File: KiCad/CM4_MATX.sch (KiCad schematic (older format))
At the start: 0 parts

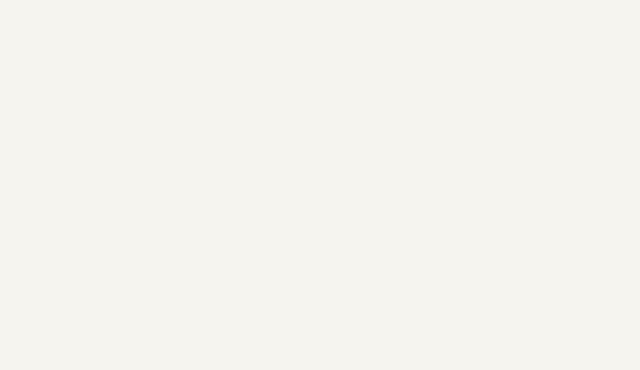
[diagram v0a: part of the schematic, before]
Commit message: added mounting holes to CM4_MATX.sch
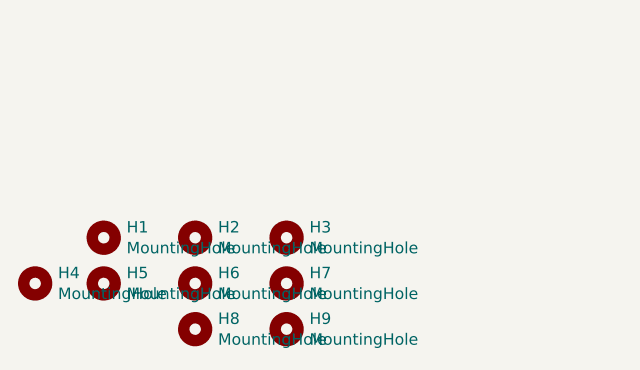
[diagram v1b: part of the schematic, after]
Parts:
- added H1, H2, H3, H4, H5, H6, H7, H8, H9: MountingHole, MountingHole:MountingHole_3.2mm_M3, symbol Mechanical:MountingHole
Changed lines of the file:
@@
 F1 "CM4_USB2_HUB.sch" 50
 $EndSheet
+$Comp
+L Mechanical:MountingHole H1
+U 1 1 5FB6444A
+P 1150 7200
+F 0 "H1" H 1250 7246 50  0000 L CNN
+F 1 "MountingHole" H 1250 7155 50  0000 L CNN
+F 2 "MountingHole:MountingHole_3.2mm_M3" H 1150 7200 50  0001 C CNN
+F 3 "~" H 1150 7200 50  0001 C CNN
+	1    1150 7200
+	1    0    0    -1
+$EndComp
+$Comp
+L Mechanical:MountingHole H2
+U 1 1 5FB649F9
+P 1550 7200
+F 0 "H2" H 1650 7246 50  0000 L CNN
+F 1 "MountingHole" H 1650 7155 50  0000 L CNN
+F 2 "MountingHole:MountingHole_3.2mm_M3" H 1550 7200 50  0001 C CNN
+F 3 "~" H 1550 7200 50  0001 C CNN
+	1    1550 7200
+	1    0    0    -1
+$EndComp
+$Comp
+L Mechanical:MountingHole H3
+U 1 1 5FB64C61
+P 1950 7200
+F 0 "H3" H 2050 7246 50  0000 L CNN
+F 1 "MountingHole" H 2050 7155 50  0000 L CNN
+F 2 "MountingHole:MountingHole_3.2mm_M3" H 1950 7200 50  0001 C CNN
+F 3 "~" H 1950 7200 50  0001 C CNN
+	1    1950 7200
+	1    0    0    -1
+$EndComp
+$Comp
+L Mechanical:MountingHole H4
+U 1 1 5FB658C2
+P 850 7400
+F 0 "H4" H 950 7446 50  0000 L CNN
+F 1 "MountingHole" H 950 7355 50  0000 L CNN
+F 2 "MountingHole:MountingHole_3.2mm_M3" H 850 7400 50  0001 C CNN
+F 3 "~" H 850 7400 50  0001 C CNN
+	1    850  7400
+	1    0    0    -1
+$EndComp
+$Comp
+L Mechanical:MountingHole H5
+U 1 1 5FB65A47
+P 1150 7400
+F 0 "H5" H 1250 7446 50  0000 L CNN
+F 1 "MountingHole" H 1250 7355 50  0000 L CNN
+F 2 "MountingHole:MountingHole_3.2mm_M3" H 1150 7400 50  0001 C CNN
+F 3 "~" H 1150 7400 50  0001 C CNN
+	1    1150 7400
+	1    0    0    -1
+$EndComp
+$Comp
+L Mechanical:MountingHole H6
+U 1 1 5FB65B17
+P 1550 7400
+F 0 "H6" H 1650 7446 50  0000 L CNN
+F 1 "MountingHole" H 1650 7355 50  0000 L CNN
+F 2 "MountingHole:MountingHole_3.2mm_M3" H 1550 7400 50  0001 C CNN
+F 3 "~" H 1550 7400 50  0001 C CNN
+	1    1550 7400
+	1    0    0    -1
+$EndComp
+$Comp
+L Mechanical:MountingHole H7
+U 1 1 5FB65D40
+P 1950 7400
+F 0 "H7" H 2050 7446 50  0000 L CNN
+F 1 "MountingHole" H 2050 7355 50  0000 L CNN
+F 2 "MountingHole:MountingHole_3.2mm_M3" H 1950 7400 50  0001 C CNN
+F 3 "~" H 1950 7400 50  0001 C CNN
+	1    1950 7400
+	1    0    0    -1
+$EndComp
+$Comp
+L Mechanical:MountingHole H9
+U 1 1 5FB65FD3
+P 1950 7600
+F 0 "H9" H 2050 7646 50  0000 L CNN
+F 1 "MountingHole" H 2050 7555 50  0000 L CNN
+F 2 "MountingHole:MountingHole_3.2mm_M3" H 1950 7600 50  0001 C CNN
+F 3 "~" H 1950 7600 50  0001 C CNN
+	1    1950 7600
+	1    0    0    -1
+$EndComp
+$Comp
+L Mechanical:MountingHole H8
+U 1 1 5FB66182
+P 1550 7600
+F 0 "H8" H 1650 7646 50  0000 L CNN
+F 1 "MountingHole" H 1650 7555 50  0000 L CNN
+F 2 "MountingHole:MountingHole_3.2mm_M3" H 1550 7600 50  0001 C CNN
+F 3 "~" H 1550 7600 50  0001 C CNN
+	1    1550 7600
+	1    0    0    -1
+$EndComp
 $EndSCHEMATC

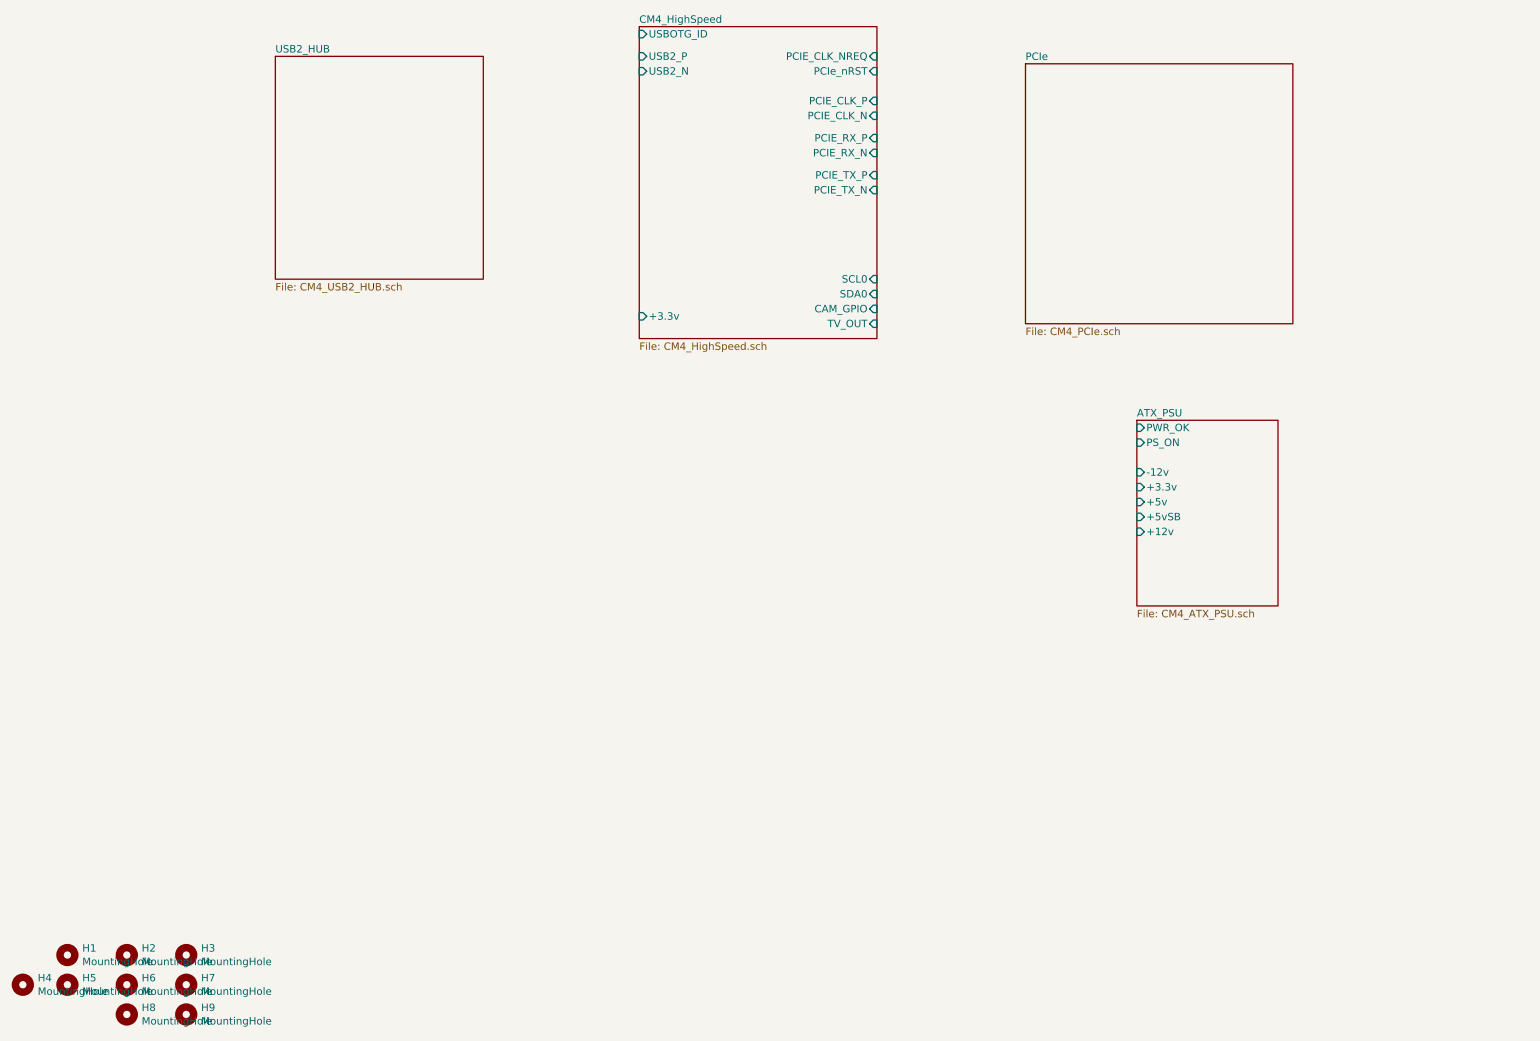
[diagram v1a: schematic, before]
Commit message: Lotsa changes
Added new footprints:
PCIe x1, TO-252 tab, SOT95, SOP50, SON50, Hirose FH-12-22S, 2.54mm 2x02 and 2x05 headers
Added new models:
Hirose FH-12-22S, FSUSB42MUX, MIC2019YM6-TR, TPS6206
Re-did ATX connector symbol wiring
Begun wiring PI7C PCI-e switch
Wired USB2517 hub
Begun adding MIC2019YM6 current limiters.
Added TODO lists to each page to help new contributors
Begun placing PCB footprints and descriptors
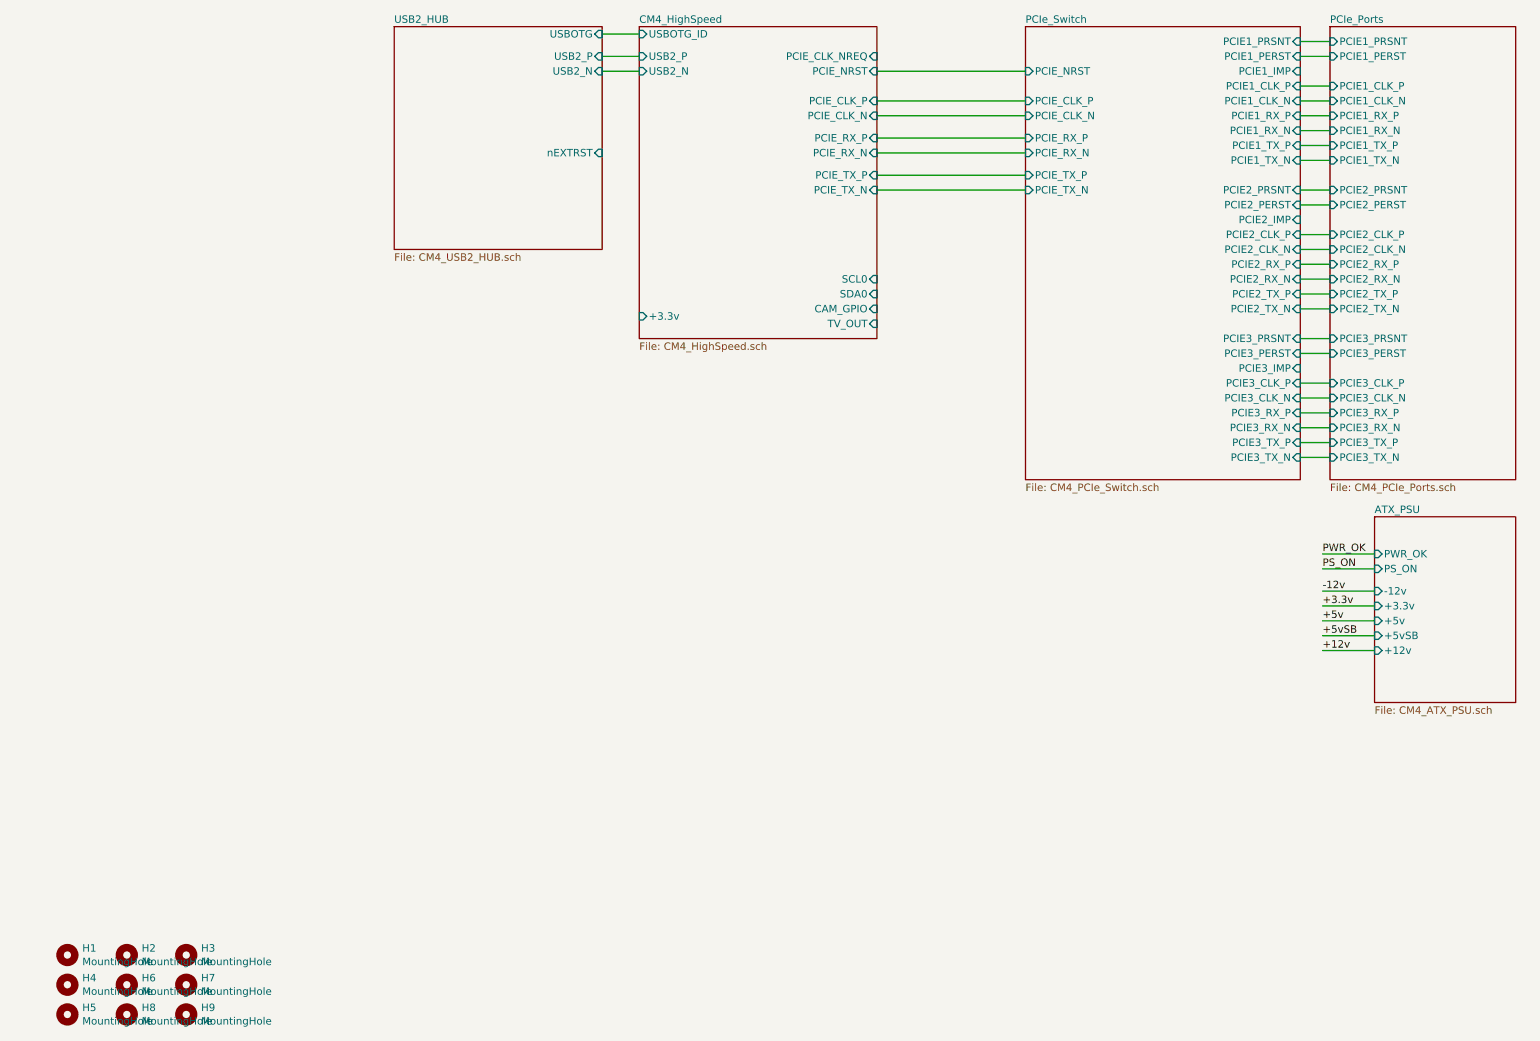
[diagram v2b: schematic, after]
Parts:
- H3: footprint MountingHole:MountingHole_3.2mm_M3 -> MountingHole:MountingHole_3.2mm_M3_Pad_Via
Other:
- moved on the sheet: H4, H5
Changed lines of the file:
@@
 $Descr A4 11693 8268
 encoding utf-8
-Sheet 1 5
+Sheet 1 6
 Title "CM4 MATX Root Sheet"
 Date "2020-11-19"
@@
 F1 "CM4_HighSpeed.sch" 50
 F2 "TV_OUT" I R 6600 2950 50
-F3 "PCIe_nRST" I R 6600 1250 50
+F3 "PCIE_NRST" I R 6600 1250 50
 F4 "USB2_P" I L 5000 1150 50
 F5 "USB2_N" I L 5000 1250 50
@@
 $EndSheet
 $Sheet
-S 8350 3600 950  1250
+S 9950 4250 950  1250
 U 5FB443D9
 F0 "ATX_PSU" 50
 F1 "CM4_ATX_PSU.sch" 50
-F2 "+3.3v" I L 8350 4050 50
-F3 "+5v" I L 8350 4150 50
-F4 "+12v" I L 8350 4350 50
-F5 "+5vSB" I L 8350 4250 50
-F6 "-12v" I L 8350 3950 50
-F7 "PS_ON" I L 8350 3750 50
-F8 "PWR_OK" I L 8350 3650 50
-$EndSheet
-$Sheet
-S 7600 1200 1800 1750
-U 5FB442B7
-F0 "PCIe" 50
-F1 "CM4_PCIe.sch" 50
-$EndSheet
-$Sheet
-S 2550 1150 1400 1500
+F2 "+3.3v" I L 9950 4850 50
+F3 "+5v" I L 9950 4950 50
+F4 "+12v" I L 9950 5150 50
+F5 "+5vSB" I L 9950 5050 50
+F6 "-12v" I L 9950 4750 50
+F7 "PS_ON" I L 9950 4600 50
+F8 "PWR_OK" I L 9950 4500 50
+$EndSheet
+$Sheet
+S 3350 950  1400 1500
 U 5FB43DAF
 F0 "USB2_HUB" 50
 F1 "CM4_USB2_HUB.sch" 50
+F2 "nEXTRST" I R 4750 1800 50
+F3 "USBOTG" I R 4750 1000 50
+F4 "USB2_P" I R 4750 1150 50
+F5 "USB2_N" I R 4750 1250 50
 $EndSheet
 $Comp
@@
 F 0 "H3" H 2050 7246 50  0000 L CNN
 F 1 "MountingHole" H 2050 7155 50  0000 L CNN
-F 2 "MountingHole:MountingHole_3.2mm_M3" H 1950 7200 50  0001 C CNN
+F 2 "MountingHole:MountingHole_3.2mm_M3_Pad_Via" H 1950 7200 50  0001 C CNN
 F 3 "~" H 1950 7200 50  0001 C CNN
 	1    1950 7200
@@
 L Mechanical:MountingHole H4
 U 1 1 5FB658C2
-P 850 7400
-F 0 "H4" H 950 7446 50  0000 L CNN
-F 1 "MountingHole" H 950 7355 50  0000 L CNN
-F 2 "MountingHole:MountingHole_3.2mm_M3" H 850 7400 50  0001 C CNN
-F 3 "~" H 850 7400 50  0001 C CNN
-	1    850  7400
-	1    0    0    -1
-$EndComp
-$Comp
-L Mechanical:MountingHole H5
-U 1 1 5FB65A47
 P 1150 7400
-F 0 "H5" H 1250 7446 50  0000 L CNN
+F 0 "H4" H 1250 7446 50  0000 L CNN
 F 1 "MountingHole" H 1250 7355 50  0000 L CNN
 F 2 "MountingHole:MountingHole_3.2mm_M3" H 1150 7400 50  0001 C CNN
 F 3 "~" H 1150 7400 50  0001 C CNN
 	1    1150 7400
+	1    0    0    -1
+$EndComp
+$Comp
+L Mechanical:MountingHole H5
+U 1 1 5FB65A47
+P 1150 7600
+F 0 "H5" H 1250 7646 50  0000 L CNN
+F 1 "MountingHole" H 1250 7555 50  0000 L CNN
+F 2 "MountingHole:MountingHole_3.2mm_M3" H 1150 7600 50  0001 C CNN
+F 3 "~" H 1150 7600 50  0001 C CNN
+	1    1150 7600
 	1    0    0    -1
 $EndComp
@@
 	1    0    0    -1
 $EndComp
+$Sheet
+S 7600 950  1850 3050
+U 5FB442B7
+F0 "PCIe_Switch" 50
+F1 "CM4_PCIe_Switch.sch" 50
+F2 "PCIE_CLK_N" I L 7600 1550 50
+F3 "PCIE_CLK_P" I L 7600 1450 50
+F4 "PCIE_RX_P" I L 7600 1700 50
+F5 "PCIE_RX_N" I L 7600 1800 50
+F6 "PCIE_TX_P" I L 7600 1950 50
+F7 "PCIE_TX_N" I L 7600 2050 50
+F8 "PCIE_NRST" I L 7600 1250 50
+F9 "PCIE1_PRSNT" I R 9450 1050 50
+F10 "PCIE2_PRSNT" I R 9450 2050 50
+F11 "PCIE3_PRSNT" I R 9450 3050 50
+F12 "PCIE1_PERST" I R 9450 1150 50
+F13 "PCIE2_PERST" I R 9450 2150 50
+F14 "PCIE3_PERST" I R 9450 3150 50
+F15 "PCIE1_IMP" I R 9450 1250 50
+F16 "PCIE2_IMP" I R 9450 2250 50
+F17 "PCIE3_IMP" I R 9450 3250 50
+F18 "PCIE3_CLK_N" I R 9450 3450 50
+F19 "PCIE3_CLK_P" I R 9450 3350 50
+F20 "PCIE2_CLK_N" I R 9450 2450 50
+F21 "PCIE2_CLK_P" I R 9450 2350 50
+F22 "PCIE1_CLK_N" I R 9450 1450 50
+F23 "PCIE1_CLK_P" I R 9450 1350 50
+F24 "PCIE1_RX_P" I R 9450 1550 50
+F25 "PCIE1_RX_N" I R 9450 1650 50
+F26 "PCIE1_TX_P" I R 9450 1750 50
+F27 "PCIE1_TX_N" I R 9450 1850 50
+F28 "PCIE2_RX_P" I R 9450 2550 50
+F29 "PCIE2_RX_N" I R 9450 2650 50
+F30 "PCIE2_TX_P" I R 9450 2750 50
+F31 "PCIE2_TX_N" I R 9450 2850 50
+F32 "PCIE3_TX_N" I R 9450 3850 50
+F33 "PCIE3_TX_P" I R 9450 3750 50
+F34 "PCIE3_RX_N" I R 9450 3650 50
+F35 "PCIE3_RX_P" I R 9450 3550 50
+$EndSheet
+Text Label 9600 4500 0    50   ~ 0
+PWR_OK
+Text Label 9600 4600 0    50   ~ 0
+PS_ON
+Text Label 9600 4850 0    50   ~ 0
++3.3v
+Text Label 9600 4950 0    50   ~ 0
++5v
+Text Label 9600 5050 0    50   ~ 0
++5vSB
+Text Label 9600 5150 0    50   ~ 0
++12v
+Wire Wire Line
+	9600 5150 9950 5150
+Wire Wire Line
+	9950 5050 9600 5050
+Wire Wire Line
+	9600 4950 9950 4950
+Wire Wire Line
+	9950 4850 9600 4850
+Wire Wire Line
+	9950 4600 9600 4600
+Wire Wire Line
+	9600 4500 9950 4500
+$Sheet
+S 9650 950  1250 3050
+U 5FCA7683
+F0 "PCIe_Ports" 50
+F1 "CM4_PCIe_Ports.sch" 50
+F2 "PCIE2_PRSNT" I L 9650 2050 50
+F3 "PCIE2_PERST" I L 9650 2150 50
+F4 "PCIE2_CLK_P" I L 9650 2350 50
+F5 "PCIE2_CLK_N" I L 9650 2450 50
+F6 "PCIE2_RX_P" I L 9650 2550 50
+F7 "PCIE2_RX_N" I L 9650 2650 50
+F8 "PCIE2_TX_N" I L 9650 2850 50
+F9 "PCIE2_TX_P" I L 9650 2750 50
+F10 "PCIE3_PRSNT" I L 9650 3050 50
+F11 "PCIE3_PERST" I L 9650 3150 50
+F12 "PCIE3_CLK_P" I L 9650 3350 50
+F13 "PCIE3_CLK_N" I L 9650 3450 50
+F14 "PCIE3_RX_N" I L 9650 3650 50
+F15 "PCIE3_RX_P" I L 9650 3550 50
+F16 "PCIE1_RX_P" I L 9650 1550 50
+F17 "PCIE1_RX_N" I L 9650 1650 50
+F18 "PCIE1_CLK_N" I L 9650 1450 50
+F19 "PCIE1_CLK_P" I L 9650 1350 50
+F20 "PCIE1_PERST" I L 9650 1150 50
+F21 "PCIE1_PRSNT" I L 9650 1050 50
+F22 "PCIE1_TX_P" I L 9650 1750 50
+F23 "PCIE1_TX_N" I L 9650 1850 50
+F24 "PCIE3_TX_P" I L 9650 3750 50
+F25 "PCIE3_TX_N" I L 9650 3850 50
+$EndSheet
+Wire Wire Line
+	9650 3850 9450 3850
+Wire Wire Line
+	9450 3750 9650 3750
+Wire Wire Line
+	9650 3650 9450 3650
+Wire Wire Line
+	9450 3550 9650 3550
+Wire Wire Line
+	9650 3450 9450 3450
+Wire Wire Line
+	9450 3350 9650 3350
+Wire Wire Line
+	9650 3150 9450 3150
+Wire Wire Line
+	9450 3050 9650 3050
+Wire Wire Line
+	9650 2850 9450 2850
+Wire Wire Line
+	9450 2750 9650 2750
+Wire Wire Line
+	9650 2650 9450 2650
+Wire Wire Line
+	9450 2550 9650 2550
+Wire Wire Line
+	9650 2450 9450 2450
+Wire Wire Line
+	9450 2350 9650 2350
+Wire Wire Line
+	9650 2150 9450 2150
+Wire Wire Line
+	9450 2050 9650 2050
+Wire Wire Line
+	9650 1850 9450 1850
+Wire Wire Line
+	9450 1750 9650 1750
+Wire Wire Line
+	9650 1650 9450 1650
+Wire Wire Line
+	9450 1550 9650 1550
+Wire Wire Line
+	9650 1450 9450 1450
+Wire Wire Line
+	9450 1350 9650 1350
+Wire Wire Line
+	9650 1150 9450 1150
+Wire Wire Line
+	9450 1050 9650 1050
+Wire Wire Line
+	7600 1250 6600 1250
+Wire Wire Line
+	6600 1450 7600 1450
+Wire Wire Line
+	7600 1550 6600 1550
+Wire Wire Line
+	6600 1700 7600 1700
+Wire Wire Line
+	7600 1800 6600 1800
+Wire Wire Line
+	6600 1950 7600 1950
+Wire Wire Line
+	7600 2050 6600 2050
+Wire Wire Line
+	4750 1250 5000 1250
+Wire Wire Line
+	5000 1150 4750 1150
+Wire Wire Line
+	4750 1000 5000 1000
+Wire Wire Line
+	9600 4750 9950 4750
+Text Label 9600 4750 0    50   ~ 0
+-12v
 $EndSCHEMATC

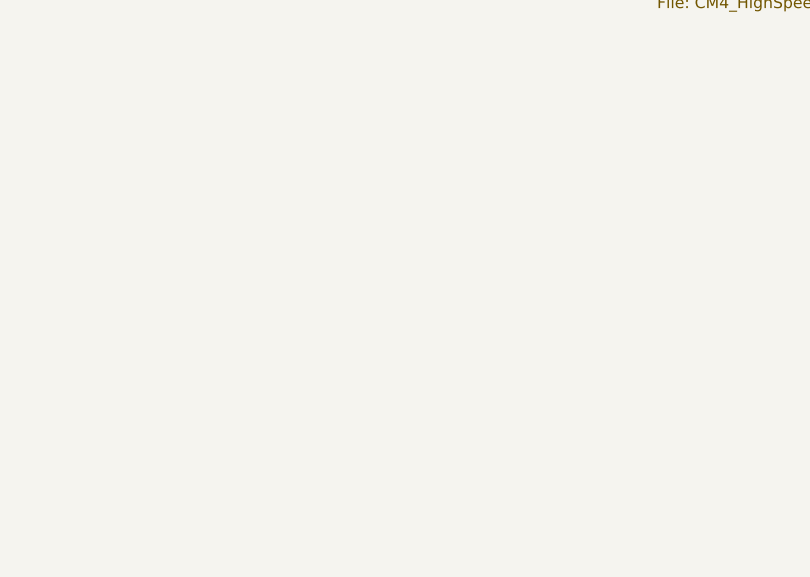
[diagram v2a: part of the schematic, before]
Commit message: added FanCRTL with MAX31740 as hierarchical sheet
with all footprints and symbols necessary
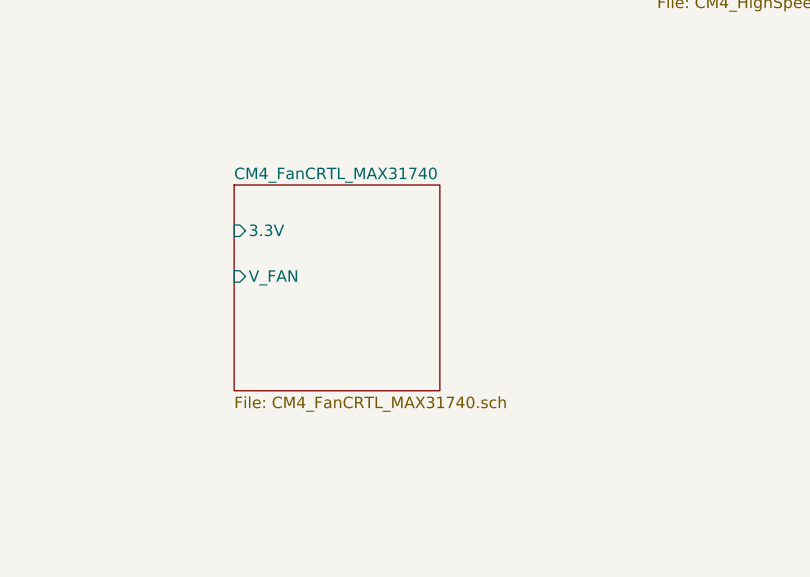
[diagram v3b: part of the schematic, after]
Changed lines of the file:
@@
 $Descr A4 11693 8268
 encoding utf-8
-Sheet 1 6
+Sheet 1 7
 Title "CM4 MATX Root Sheet"
 Date "2020-11-19"
@@
 Text Label 9600 4750 0    50   ~ 0
 -12v
+$Sheet
+S 3150 3900 900  900
+U 5FBAD4A8
+F0 "CM4_FanCRTL_MAX31740" 50
+F1 "CM4_FanCRTL_MAX31740.sch" 50
+F2 "3.3V" I L 3150 4100 50
+F3 "V_FAN" I L 3150 4300 50
+$EndSheet
 $EndSCHEMATC
